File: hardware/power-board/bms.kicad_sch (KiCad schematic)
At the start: 1 part, among them IC2 BQ7694202PFBR

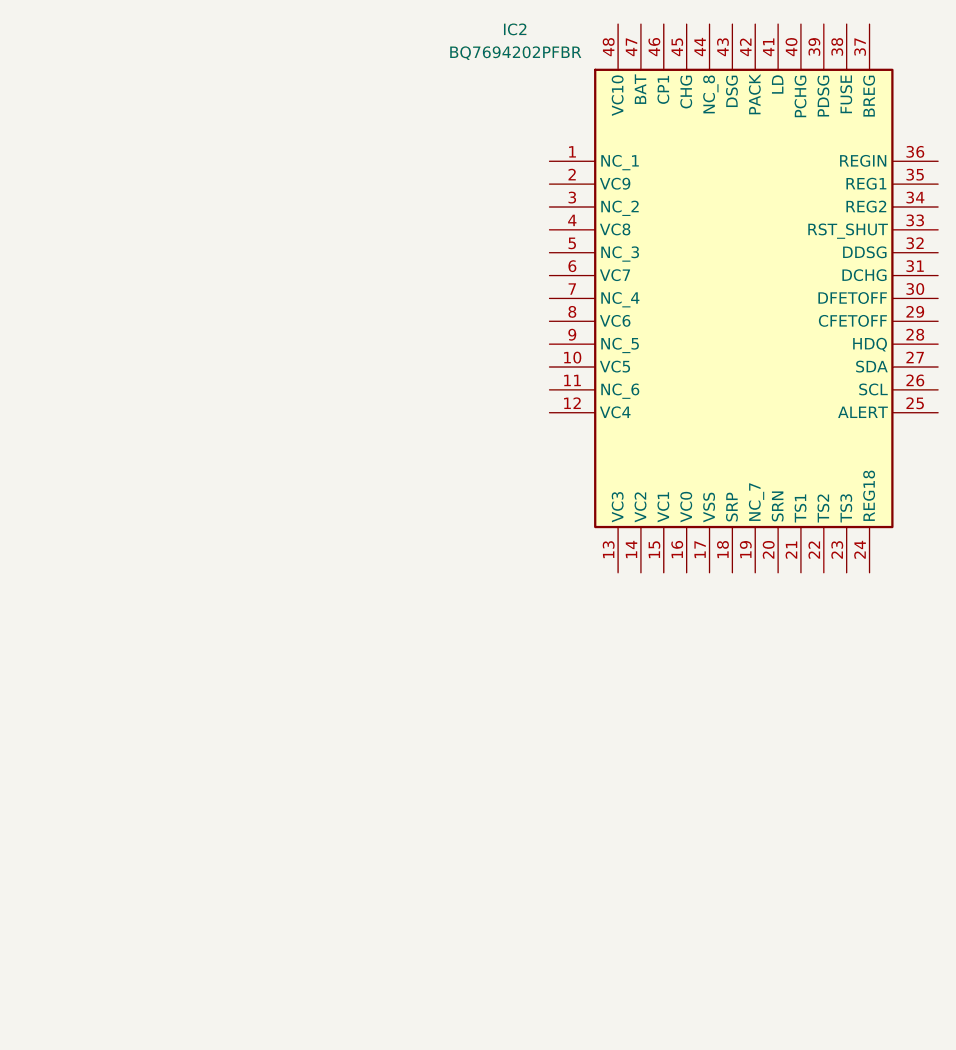
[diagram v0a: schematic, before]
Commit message: Added more ICs for power board
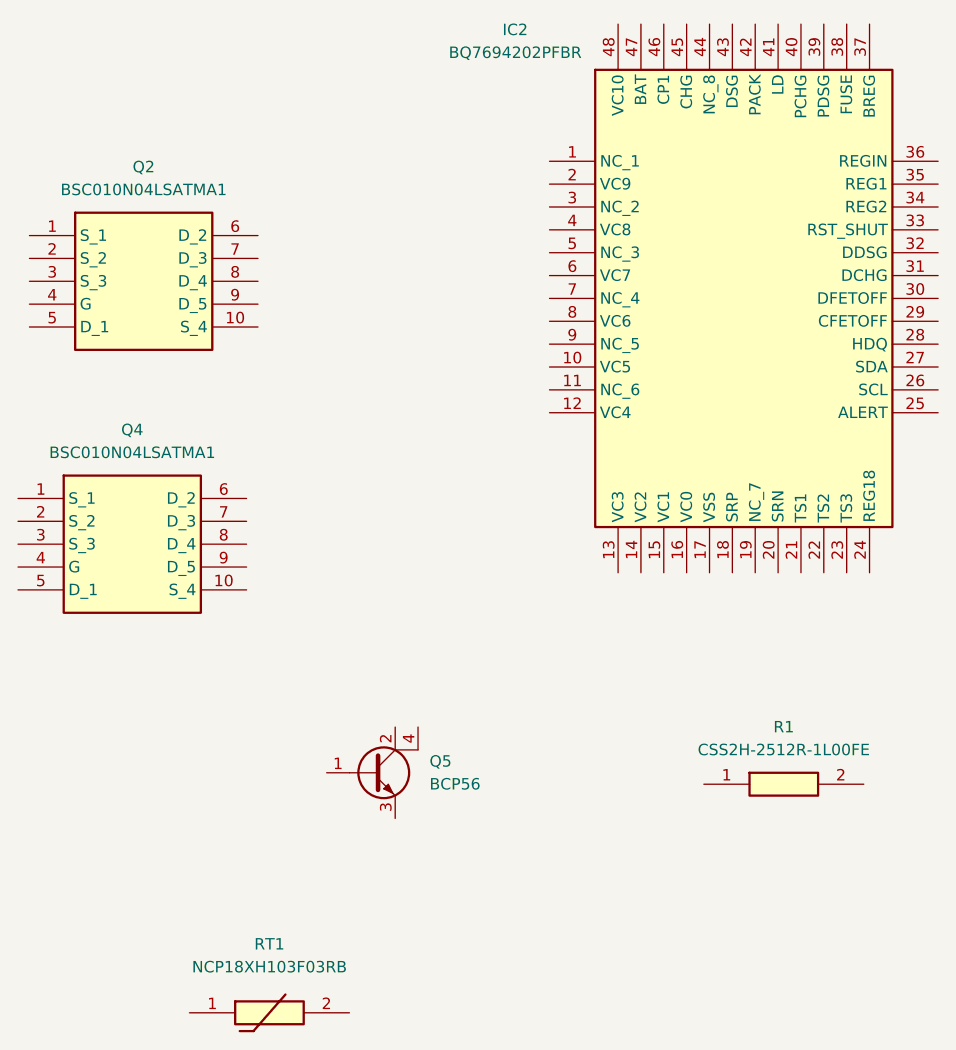
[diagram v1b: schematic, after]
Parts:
- added Q2, Q4: BSC010N04LSATMA1, power-board:BSC010N04LSATMA1, symbol power-board:BSC010N04LSATMA1
- added Q5: BCP56, Package_TO_SOT_SMD:SOT-223-3_TabPin2, symbol Transistor_BJT:BCP56
- added R1: CSS2H-2512R-1L00FE, power-board:CSS2H2512R1L00FE, symbol power-board:CSS2H-2512R-1L00FE
- added RT1: NCP18XH103F03RB, vector:THRMC1608X95N, symbol vector:NCP18XH103F03RB

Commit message: draw power board bms, charger and mcu circuits
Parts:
- added C301, C305: 1u, Capacitor_SMD:C_0805_2012Metric, symbol Device:C
- added C302: 470n, Capacitor_SMD:C_0805_2012Metric, symbol Device:C
- added C303, C304: 2.2u, Capacitor_SMD:C_0805_2012Metric, symbol Device:C
- added C306: 100n, Capacitor_SMD:C_0805_2012Metric, symbol Device:C
- added C307, C308, C309, C310, C311: 220n, Capacitor_SMD:C_0805_2012Metric, symbol Device:C
- added C312: 100u 35V, Capacitor_SMD:CP_Elec_8x10.5, symbol Device:C_Polarized
- added D301, D302: 1N4148W, Diode_SMD:D_SOD-123, symbol Device:D
- added D303: SMBJ18A, Diode_SMD:D_SMB, symbol Device:D_TVS
- added D304: BAT54J, Diode_SMD:D_SOD-323F, symbol Device:D_Schottky
- added J301: XT60 BAT, Connector_AMASS:AMASS_XT60PW-M_1x02_P7.20mm_Horizontal, symbol Connector_Generic:Conn_01x02
- added J302: BALANCE, Connector_JST:JST_XH_B5B-XH-A_1x05_P2.50mm_Vertical, symbol Connector_Generic:Conn_01x05
- added J303: NTC CELL, Connector_JST:JST_PH_B2B-PH-K_1x02_P2.00mm_Vertical, symbol Connector_Generic:Conn_01x02
- added J304: POWER BTN, Connector_JST:JST_PH_B2B-PH-K_1x02_P2.00mm_Vertical, symbol Connector_Generic:Conn_01x02
- added J305: XT30 LEFT, Connector_AMASS:AMASS_XT30PW-M_1x02_P2.50mm_Horizontal, symbol Connector_Generic:Conn_01x02
- added J306: XT30 RIGHT, Connector_AMASS:AMASS_XT30PW-M_1x02_P2.50mm_Horizontal, symbol Connector_Generic:Conn_01x02
- added J307: XT30 CARRIER, Connector_AMASS:AMASS_XT30PW-M_1x02_P2.50mm_Horizontal, symbol Connector_Generic:Conn_01x02
- added Q301: DMP3099L, Package_TO_SOT_SMD:SOT-23, symbol Transistor_FET:TP0610T
- added R301, R303, R304, R310, R312: 100, Resistor_SMD:R_0603_1608Metric, symbol Device:R
- added R302, R311, R313: 10M, Resistor_SMD:R_0603_1608Metric, symbol Device:R
- added R305, R306, R307, R308, R309: 20, Resistor_SMD:R_0603_1608Metric, symbol Device:R
- added R314, R315, R317: 10k, Resistor_SMD:R_0603_1608Metric, symbol Device:R
- added R316: 100k, Resistor_SMD:R_0603_1608Metric, symbol Device:R
- added R318: 100 2W, Resistor_SMD:R_2512_6332Metric, symbol Device:R
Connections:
- net VC3: now reaches IC2.10 (VC5)
- net VC3: now also IC2.12 (VC4), IC2.13 (VC3), IC2.2 (VC9), IC2.4 (VC8), IC2.6 (VC7), IC2.8 (VC6), C310.1, C311.2, R308.2
- net VC2: now reaches IC2.14 (VC2)
- net VC2: now also C309.1, C310.2, R307.2
- net VC1: now reaches IC2.15 (VC1)
- net VC1: now also C308.1, C309.2, R306.2
- net VC0: now reaches IC2.16 (VC0)
- net VC0: now also C307.1, C308.2, R305.2
- net BAT-: now reaches IC2.17 (VSS)
- net BAT-: now also IC2.33 (RST_SHUT), R1.1, RT1.2, C301.2, C303.2, C304.2, C305.2, C307.2, J301.2 (Pin_2), J303.2 (Pin_2), J304.2 (Pin_2), R302.2, R303.1
- net BMS_SRP: now reaches IC2.18 (SRP)
- net BMS_SRP: now also C306.1, R303.2
- net BMS_SRN: now reaches IC2.20 (SRN)
- net BMS_SRN: now also C306.2, R304.1
- net NTC_CELL: now reaches IC2.21 (TS1)
- net NTC_CELL: now also J303.1 (Pin_1)
- net TS2_WAKE: now reaches IC2.22 (TS2)
- net TS2_WAKE: now also D304.2 (A)
- net NTC_FET: now reaches IC2.23 (TS3)
- net NTC_FET: now also RT1.1
- net BMS_REG18: now reaches IC2.24 (REG18)
- net BMS_REG18: now also C305.1
- net BMS_ALERT: now reaches IC2.25 (ALERT)
- net I2C_SCL: now reaches IC2.26 (SCL)
- net I2C_SDA: now reaches IC2.27 (SDA)
- net REG1: now reaches IC2.35 (REG1)
- net REG1: now also C304.1
- net BMS_REGIN: now reaches IC2.36 (REGIN)
- net BMS_REGIN: now also Q5.3 (E), C303.1
- net BMS_BREG: now reaches IC2.37 (BREG)
- net BMS_BREG: now also Q5.1 (B), R302.1
- net BMS_PDSG: now reaches IC2.39 (PDSG)
- net BMS_PDSG: now also R317.1
- net BMS_LD: now reaches IC2.41 (LD)
- net BMS_LD: now also R315.1
- net BMS_PACK: now reaches IC2.42 (PACK)
- net BMS_PACK: now also R314.1
- net BMS_DSG: now reaches IC2.43 (DSG)
- net BMS_DSG: now also R312.1
- net BMS_CHG: now reaches IC2.45 (CHG)
- net BMS_CHG: now also R310.1
- net BMS_CP1: now reaches IC2.46 (CP1)
- net BMS_CP1: now also C302.1
- net BMS_BAT: now reaches IC2.47 (BAT)
- net BMS_BAT: now also C301.1, C302.2, R301.2
- net VC10: now reaches IC2.48 (VC10)
- net VC10: now also C311.1, R309.2
- net GND: now reaches R1.2
- net GND: now also C312.2, D303.1 (A1), J305.2 (Pin_2), J306.2 (Pin_2), J307.2 (Pin_2), R304.2
- net BMS_REG0_C: now reaches Q5.2 (C)
- net BMS_REG0_C: now also Q5.4 (C), D302.1 (K)
- net PACK+: now reaches Q4.1 (S_1)
- net PACK+: now also Q4.10 (S_4), Q4.2 (S_2), Q4.3 (S_3), C312.1, D303.2 (A2), J305.1 (Pin_1), J306.1 (Pin_1), J307.1 (Pin_1), R313.2, R314.2, R315.2, R318.2
- net DSG_G: now reaches Q4.4 (G)
- net DSG_G: now also R312.2, R313.1
- net FET_MID: now reaches Q4.5 (D_1)
- net FET_MID: now also Q2.5 (D_1), Q2.6 (D_2), Q2.7 (D_3), Q2.8 (D_4), Q2.9 (D_5), Q4.6 (D_2), Q4.7 (D_3), Q4.8 (D_4), Q4.9 (D_5), Q301.2 (S), R316.1
- net BAT+: now reaches Q2.1 (S_1)
- net BAT+: now also Q2.10 (S_4), Q2.2 (S_2), Q2.3 (S_3), D301.2 (A), D302.2 (A), J301.1 (Pin_1), R311.2
- net CHG_G: now reaches Q2.4 (G)
- net CHG_G: now also R310.2, R311.1
- new net BMS_BAT_D: D301.1 (K), R301.1
- new net BTN_N: D304.1 (K), J304.1 (Pin_1)
- new net CELL0: J302.1 (Pin_1), R305.1
- new net CELL1: J302.2 (Pin_2), R306.1
- new net CELL2: J302.3 (Pin_3), R307.1
- new net CELL3: J302.4 (Pin_4), R308.1
- new net CELL4: J302.5 (Pin_5), R309.1
- new net PDSG_D: Q301.3 (D), R318.1
- new net PDSG_G: Q301.1 (G), R316.2, R317.2
- no-connect marks 0 -> 16
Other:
- note added: "BMS Supply"
- note added: "Battery"
- note added: "Battery Monitor"
- note added: "Cell Inputs"
- note added: "Current Sense"
- note added: "Outputs"
- note added: "Protection FETs"
- moved on the sheet: IC2, Q2, Q4, Q5, R1, RT1

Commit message: Reset annotations for power board
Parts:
- renumbered C307 to C201, C308 to C202, C309 to C203, C310 to C204, C311 to C205, C312 to C206, C301 to C207, C302 to C208, C306 to C209, C303 to C210, C304 to C211, C305 to C212, D304 to D201, D303 to D202, D301 to D203, D302 to D204, IC2 to IC201, J301 to J201, J302 to J202, J303 to J203, J304 to J204, J305 to J205, J306 to J206, J307 to J207, Q2 to Q201, Q301 to Q202, Q4 to Q203, Q5 to Q204, R305 to R201, R310 to R202, R314 to R203, R306 to R204, R311 to R205, R315 to R206, R307 to R207, R308 to R208, R309 to R209, R316 to R210, R312 to R211, R317 to R212, R313 to R213, R318 to R214, R1 to R215, R301 to R216, R303 to R217, R304 to R218, R302 to R219, RT1 to RT201
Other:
- moved on the sheet: Q202, R202, R203, R205, R206, R210, R211, R212, R213, R214

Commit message: power board: test points
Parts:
- added TP301: BAT+, TestPoint:TestPoint_Pad_D2.0mm, symbol Connector:TestPoint
- added TP302: BAT-, TestPoint:TestPoint_Pad_D2.0mm, symbol Connector:TestPoint
- added TP303: PACK+, TestPoint:TestPoint_Pad_D2.0mm, symbol Connector:TestPoint
- added TP304: REG1, TestPoint:TestPoint_Pad_D2.0mm, symbol Connector:TestPoint
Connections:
- net BAT+: now also TP301.1
- net BAT-: now also TP302.1
- net PACK+: now also TP303.1
- net REG1: now also TP304.1

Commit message: power board: amrm inductor, sot-223 for q204, 2.2k i2c pull-ups, 50 v charger caps, xh connectors
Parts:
- Q204: footprint Package_TO_SOT_SMD:SOT-223-3_TabPin2 -> Package_TO_SOT_SMD:SOT-223
